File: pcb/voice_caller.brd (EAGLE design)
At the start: 100 x 80 mm, 13 parts, among them IC1 MEGA8-AI, IC2 78L12SMD, U1 AT45DB321D-S, X2 RJ45-8L-B

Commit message: Who knows
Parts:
- removed C4: (no value), rcl:C1206K
- removed IC1: MEGA8-AI, atmel:TQFP32-08
- removed R3: 220, rcl:M1206
- U$1: value MAX4544-EUTSOT23-6 -> NANO-NOISP; device max4544:SOT23-6L -> Arduino-clone:NANO-NOISP
- moved U$1 28.1 mm to (-9.80, 20.2)
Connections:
- removed net AUDIO: U$1.6
- removed net AVCC: IC1.18
- removed net MIC_IN: U$1.4
- removed net MIC_OUT: U$1.5
- removed net MIC_SWITCH: U$1.1
- removed net N$2: C4.1, R3.1, U$1.2
- net +5V: no longer IC1.4, IC1.6, R3.2
- net FLASH_CS: no longer IC1.14
- net GND: no longer C4.2, IC1.21, IC1.3, IC1.5, U$1.3
- net MISO: no longer IC1.16
- net MOSI: no longer IC1.15
- net SCK: no longer IC1.17
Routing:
- net GND: track 39.8 -> 10.6 mm
- net SCK: track 15.2 -> 6.50 mm
- net +5V: track 15.5 -> 9.25 mm
- net MISO: track 14.5 -> 8.95 mm
- net FLASH_CS: track 26.2 -> 22.6 mm
- net MOSI: track 17.9 -> 15.6 mm
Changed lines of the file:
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@@
 <?xml version="1.0" encoding="utf-8"?>
 <!DOCTYPE eagle SYSTEM "eagle.dtd">
-<eagle version="7.1.0">
+<eagle version="7.7.0">
 <drawing>
 <settings>
@@
 <element name="C1" library="rcl" package="C1206K" value="" x="26.36" y="45.6" rot="R90"/>
 <element name="C2" library="rcl" package="C1206K" value="" x="51.579403125" y="30.948178125" rot="R270"/>
-<element name="IC1" library="atmel" package="TQFP32-08" value="MEGA8-AI" x="29.43" y="31">
-<attribute name="OC_NEWARK" value="73M8863" x="29.43" y="31" size="1.778" layer="27" display="off"/>
-<attribute name="MPN" value="ATMEGA8-16AU" x="29.43" y="31" size="1.778" layer="27" display="off"/>
-<attribute name="MF" value="" x="29.43" y="31" size="1.778" layer="27" display="off"/>
-<attribute name="OC_FARNELL" value="9171371" x="29.43" y="31" size="1.778" layer="27" display="off"/>
-</element>
 <element name="U1" library="memory-atmel" package="SO08-8S2" value="AT45DB321D-S" x="47.02" y="31.05"/>
 <element name="CONN_RADIO" library="con-tycoelectronics" package="RJ45-NO-SHIELD" value="RJ45-8L-B" x="18.59" y="56.51" rot="R180">
@@
 <element name="R1" library="rcl" package="M1206" value="3k9" x="41.4" y="40.8"/>
 <element name="R2" library="rcl" package="M1206" value="2k2" x="28.4" y="40.8" rot="R180"/>
-<element name="U$1" library="max4544" package="SOT23-6L" value="MAX4544-EUTSOT23-6" x="14.6" y="34.2"/>
-<element name="R3" library="rcl" package="M1206" value="220" x="18.8" y="20.8"/>
-<element name="C4" library="rcl" package="C1206K" value="" x="12.2" y="22.2" rot="R180"/>
+<element name="U$1" library="Arduino-clone" package="NANO-NOISP" value="NANO-NOISP" x="-9.8" y="20.2"/>
 </elements>
 <signals>
-<signal name="AVCC">
-<contactref element="IC1" pad="18"/>
-</signal>
 <signal name="+5V">
-<contactref element="IC1" pad="4"/>
-<contactref element="IC1" pad="6"/>
 <contactref element="C2" pad="1"/>
 <contactref element="U1" pad="6"/>
-<wire x1="25.1374" y1="29.8" x2="22" y2="29.8" width="0.4064" layer="1"/>
 <wire x1="22" y1="29.8" x2="22" y2="31.4" width="0.4064" layer="1"/>
-<wire x1="22" y1="31.4" x2="25.1374" y2="31.4" width="0.4064" layer="1"/>
 <contactref element="C3" pad="1"/>
 <wire x1="20.2" y1="29.5" x2="21.7" y2="29.5" width="0.4064" layer="1"/>
@@
 <wire x1="48.551821875" y1="32.448178125" x2="47.655" y2="33.345" width="0.4064" layer="1"/>
 <wire x1="47.655" y1="34.775" x2="47.655" y2="33.345" width="0.4064" layer="1"/>
-<contactref element="R3" pad="2"/>
-<wire x1="25.1374" y1="31.4" x2="47.655" y2="33.345" width="0" layer="19" extent="1-1"/>
-<wire x1="20.2" y1="20.8" x2="20.2" y2="29.5" width="0" layer="19" extent="1-1"/>
+<wire x1="22" y1="31.4" x2="47.655" y2="33.345" width="0" layer="19" extent="1-1"/>
 </signal>
 <signal name="GND">
-<contactref element="IC1" pad="3"/>
-<contactref element="IC1" pad="5"/>
 <contactref element="C1" pad="2"/>
 <contactref element="C2" pad="2"/>
-<contactref element="IC1" pad="21"/>
 <contactref element="U1" pad="7"/>
-<wire x1="25.1374" y1="30.6" x2="27.8" y2="30.6" width="0.4064" layer="1"/>
-<wire x1="27.8" y1="30.6" x2="27.8" y2="31.4" width="0.4064" layer="1"/>
-<wire x1="27.8" y1="31.4" x2="27.8" y2="32.2" width="0.4064" layer="1"/>
-<wire x1="27.8" y1="32.2" x2="25.1374" y2="32.2" width="0.4064" layer="1"/>
-<wire x1="33.7226" y1="31.4" x2="27.8" y2="31.4" width="0.4064" layer="1"/>
-<wire x1="33.7226" y1="31.4" x2="45.4" y2="31.4" width="0.4064" layer="1"/>
 <wire x1="45.4" y1="31.4" x2="46.385" y2="32.385" width="0.4064" layer="1"/>
 <wire x1="46.385" y1="34.775" x2="46.385" y2="32.385" width="0.4064" layer="1"/>
 <contactref element="C3" pad="2"/>
-<wire x1="25.1374" y1="32.2" x2="20.5" y2="32.2" width="0.4064" layer="1"/>
 <wire x1="20.5" y1="32.2" x2="20.2" y2="32.5" width="0.4064" layer="1"/>
 <wire x1="51.579403125" y1="29.448178125" x2="49.321821875" y2="29.448178125" width="0.4064" layer="1"/>
@@
 <contactref element="CONN_RADIO" pad="7"/>
 <contactref element="CONN_RADIO" pad="5"/>
-<contactref element="U$1" pad="3"/>
-<contactref element="C4" pad="2"/>
 <wire x1="55.965" y1="43.8" x2="57.235" y2="43.8" width="0" layer="19" extent="1-1"/>
-<wire x1="57.235" y1="38.6" x2="57.235" y2="43.8" width="0" layer="19" extent="1-1"/>
-<wire x1="55.965" y1="38.6" x2="57.235" y2="38.6" width="0" layer="19" extent="1-1"/>
-<wire x1="46.385" y1="34.775" x2="55.965" y2="38.6" width="0" layer="19" extent="1-1"/>
-<wire x1="17.955" y1="50.16" x2="55.965" y2="43.8" width="0" layer="19" extent="1-1"/>
+<wire x1="55.965" y1="38.6" x2="55.965" y2="43.8" width="0" layer="19" extent="1-1"/>
+<wire x1="57.235" y1="38.6" x2="55.965" y2="38.6" width="0" layer="19" extent="1-1"/>
+<wire x1="51.579403125" y1="29.448178125" x2="55.965" y2="38.6" width="0" layer="19" extent="1-1"/>
+<wire x1="26.36" y1="47.1" x2="46.385" y2="34.775" width="0" layer="19" extent="1-1"/>
+<wire x1="17.955" y1="50.16" x2="26.36" y2="47.1" width="0" layer="19" extent="1-1"/>
 <wire x1="15.415" y1="50.16" x2="17.955" y2="50.16" width="0" layer="19" extent="1-1"/>
-<wire x1="26.36" y1="47.1" x2="15.415" y2="50.16" width="0" layer="19" extent="1-1"/>
-<wire x1="15.55" y1="32.9" x2="20.2" y2="32.5" width="0" layer="19" extent="1-1"/>
-<wire x1="10.7" y1="22.2" x2="15.55" y2="32.9" width="0" layer="19" extent="1-1"/>
+<wire x1="20.2" y1="32.5" x2="26.36" y2="47.1" width="0" layer="19" extent="1-1"/>
 </signal>
 <signal name="VCC">
@@
 </signal>
 <signal name="MOSI">
-<contactref element="IC1" pad="15"/>
 <contactref element="U1" pad="1"/>
 <wire x1="45.115" y1="27.325" x2="45.125" y2="27.325" width="0.4064" layer="1"/>
@@
 <wire x1="41.4" y1="23.6" x2="32.2" y2="23.6" width="0.4064" layer="1"/>
 <wire x1="32.2" y1="23.6" x2="31.43" y2="24.37" width="0.4064" layer="1"/>
-<wire x1="31.43" y1="26.7074" x2="31.43" y2="24.37" width="0.4064" layer="1"/>
 </signal>
 <signal name="MISO">
-<contactref element="IC1" pad="16"/>
 <contactref element="U1" pad="8"/>
-<wire x1="32.23" y1="26.7074" x2="37.1074" y2="26.7074" width="0.4064" layer="1"/>
-<wire x1="37.1074" y1="26.7074" x2="37.6" y2="27.2" width="0.4064" layer="1"/>
 <wire x1="45.115" y1="34.775" x2="45.115" y2="33.715" width="0.4064" layer="1"/>
 <wire x1="45.115" y1="33.715" x2="44.6" y2="33.2" width="0.4064" layer="1"/>
 <wire x1="44.6" y1="33.2" x2="38" y2="33.2" width="0.4064" layer="1"/>
 <wire x1="38" y1="33.2" x2="37.6" y2="32.8" width="0.4064" layer="1"/>
-<wire x1="37.6" y1="27.2" x2="37.6" y2="32.8" width="0" layer="19" extent="1-1"/>
 </signal>
 <signal name="SCK">
-<contactref element="IC1" pad="17"/>
 <contactref element="U1" pad="2"/>
-<wire x1="33.7226" y1="28.2" x2="42.4" y2="28.2" width="0.4064" layer="1"/>
 <wire x1="42.4" y1="28.2" x2="43.8" y2="29.6" width="0.4064" layer="1"/>
 <wire x1="43.8" y1="29.6" x2="45.8" y2="29.6" width="0.4064" layer="1"/>
@@
 <signal name="FLASH_CS">
 <contactref element="U1" pad="4"/>
-<contactref element="IC1" pad="14"/>
 <wire x1="48.925" y1="27.325" x2="48.925" y2="23.925" width="0.4064" layer="1"/>
 <wire x1="48.925" y1="23.925" x2="47.4" y2="22.4" width="0.4064" layer="1"/>
 <wire x1="47.4" y1="22.4" x2="31.4" y2="22.4" width="0.4064" layer="1"/>
 <wire x1="31.4" y1="22.4" x2="30.63" y2="23.17" width="0.4064" layer="1"/>
-<wire x1="30.63" y1="26.7074" x2="30.63" y2="23.17" width="0.4064" layer="1"/>
 </signal>
 <signal name="N$7">
@@
 <contactref element="R1" pad="2"/>
 </signal>
-<signal name="N$2">
-<contactref element="U$1" pad="2"/>
-<contactref element="R3" pad="1"/>
-<contactref element="C4" pad="1"/>
-<wire x1="17.4" y1="20.8" x2="13.7" y2="22.2" width="0" layer="19" extent="1-1"/>
-<wire x1="14.6" y1="32.9" x2="17.4" y2="20.8" width="0" layer="19" extent="1-1"/>
-</signal>
-<signal name="MIC_OUT">
-<contactref element="U$1" pad="5"/>
-</signal>
-<signal name="MIC_SWITCH">
-<contactref element="U$1" pad="1"/>
-</signal>
-<signal name="AUDIO">
-<contactref element="U$1" pad="6"/>
-</signal>
-<signal name="MIC_IN">
-<contactref element="U$1" pad="4"/>
-</signal>
 <signal name="N$1">

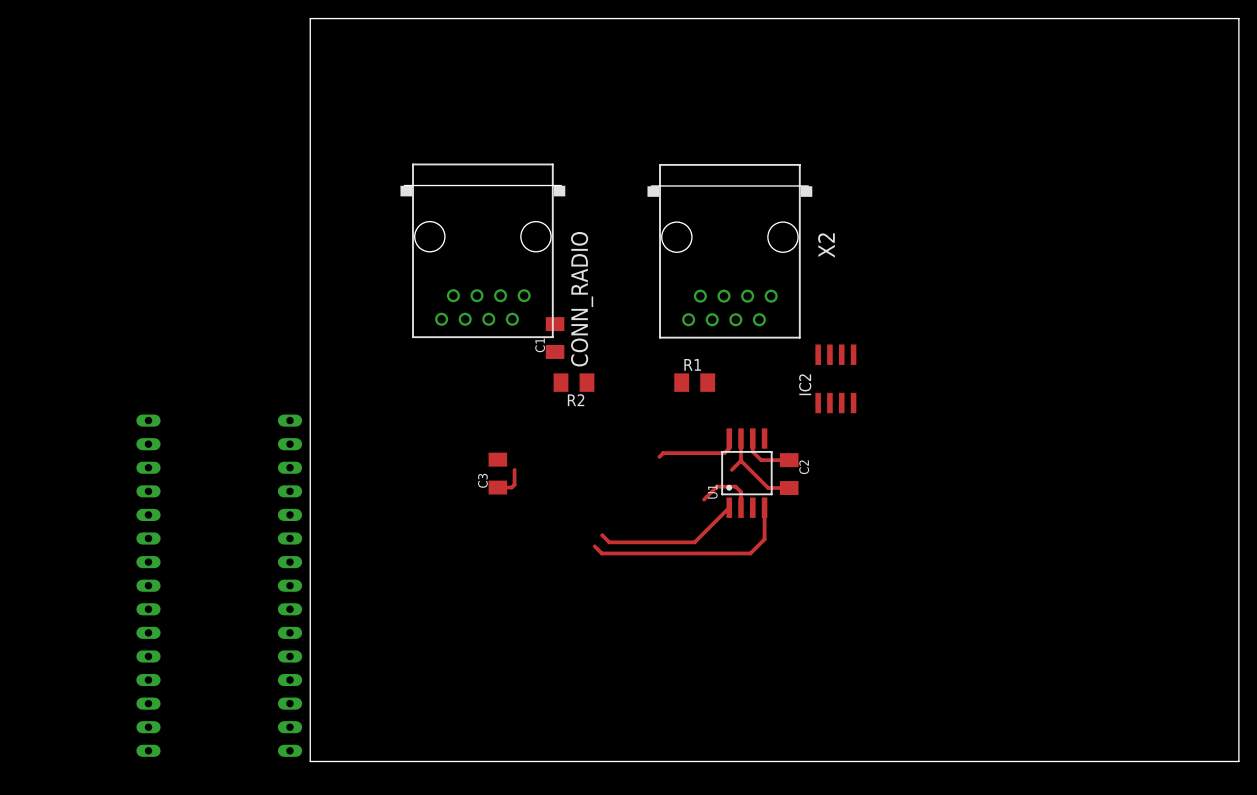
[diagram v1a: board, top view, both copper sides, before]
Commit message: Nano changed to pro micro
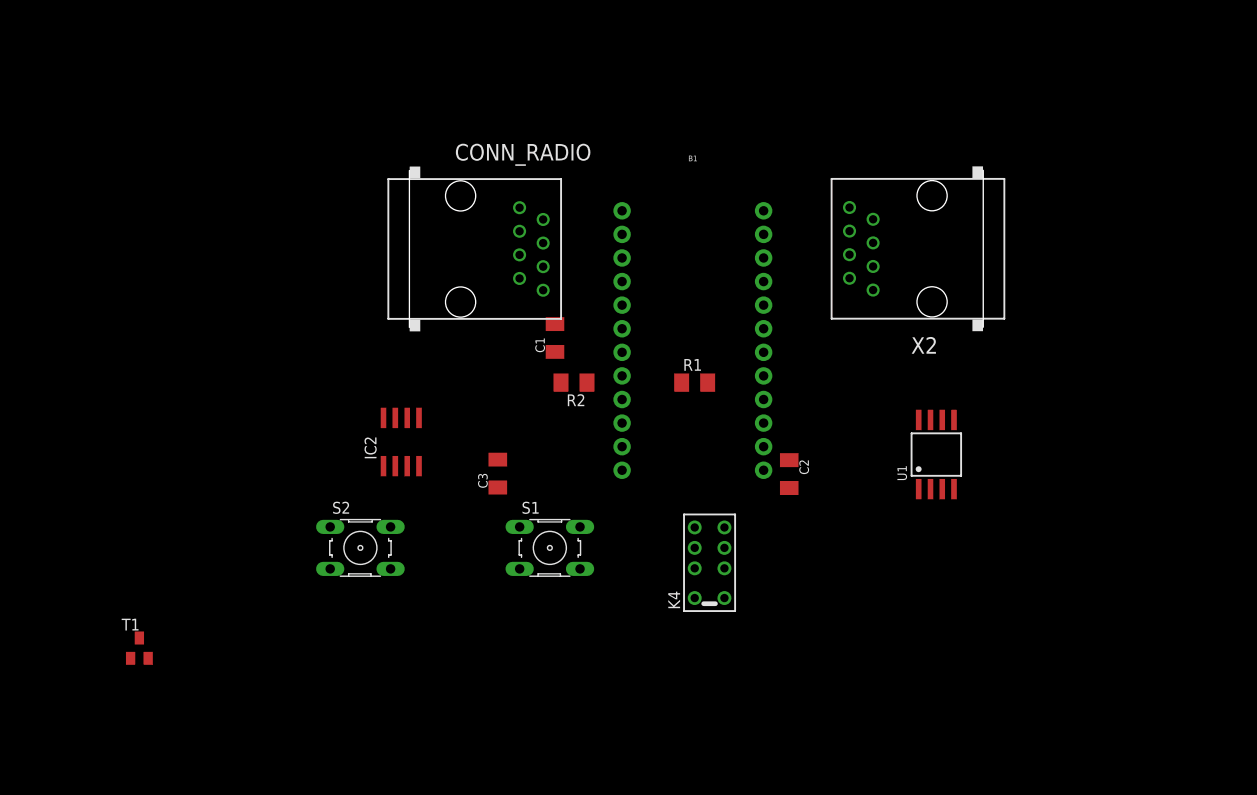
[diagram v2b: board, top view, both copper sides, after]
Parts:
- removed U$1: NANO-NOISP, Arduino-clone:NANO-NOISP
- added B1: SPARKFUN_PRO_MICRO, SparkFun-Boards:SPARKFUN_PRO_MICRO
- added K4: G6J-2P-Y, relay:G6J-2P-Y
- added S1, S2: (no value), switch-omron:B3F-10XX
- added T1: (no value), transistor:SOT23-BEC
- moved IC2 47.3 mm to (9.80, 34.4)
- moved X2 21.8 mm to (67.0, 55.2), turned to 90 degrees
- moved U1 20.5 mm to (67.4, 33.0)
- moved CONN_RADIO 2.74 mm to (16.2, 55.2), turned to 270 degrees
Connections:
- new net RAW: B1.24
- net +5V: no longer U1.6
- net GND: now also B1.23, B1.3, B1.4, S1.3, S1.4, S2.3, S2.4
- net MISO: now also B1.15
- net MOSI: now also B1.14
- net SCK: now also B1.16
- net VCC: now also B1.21, U1.6
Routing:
- net FLASH_CS: track 22.6 -> 0.00 mm
- net MOSI: track 15.6 -> 0.00 mm
- net GND: track 10.6 -> 0.42 mm
- net +5V: track 9.25 -> 0.00 mm
- net MISO: track 8.95 -> 0.00 mm
- net SCK: track 6.50 -> 0.00 mm
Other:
- board outline removed

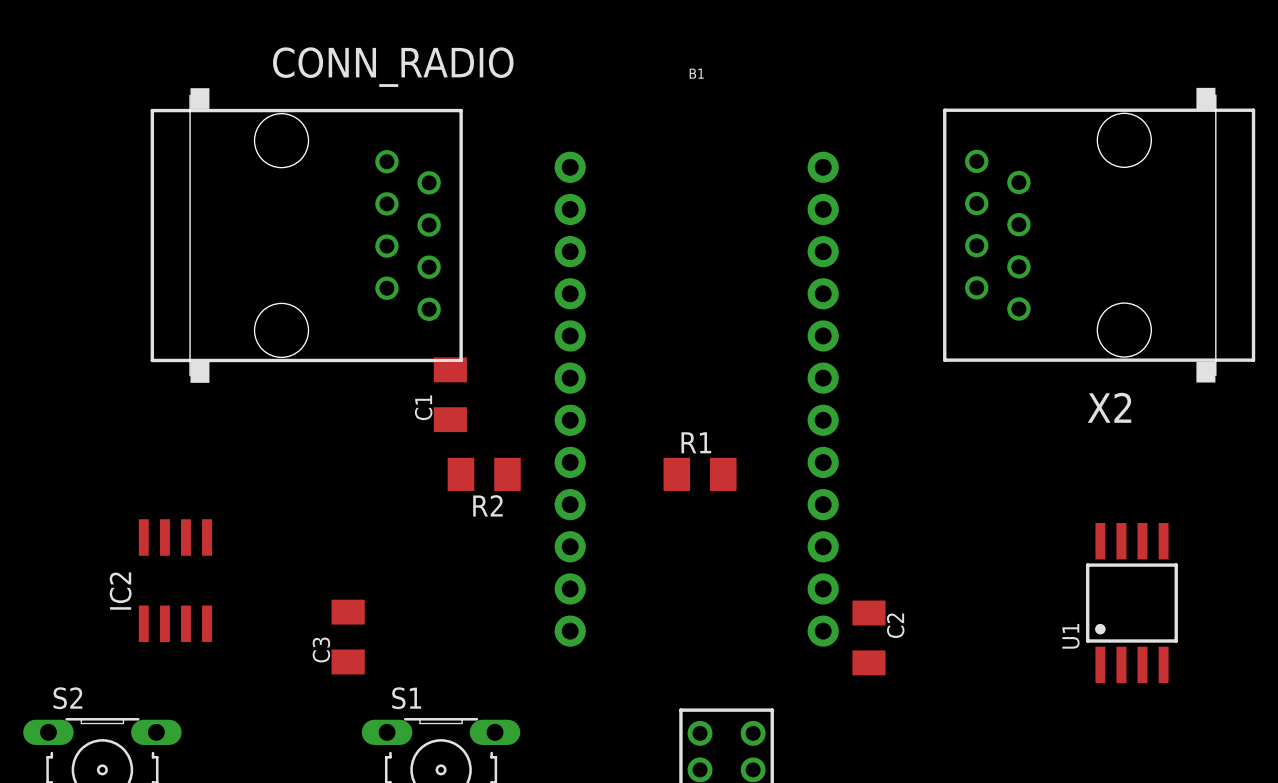
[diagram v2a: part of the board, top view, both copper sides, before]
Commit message: RJ-45 connected
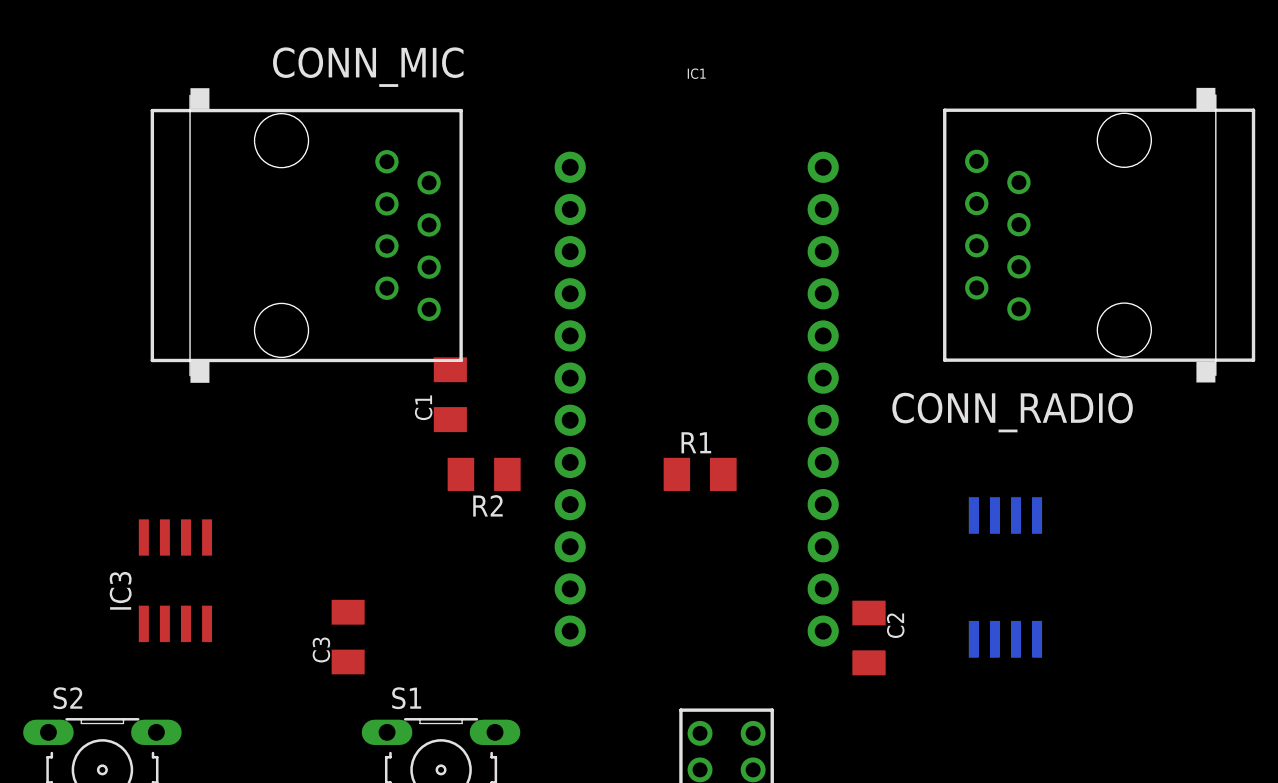
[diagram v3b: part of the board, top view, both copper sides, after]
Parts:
- removed U1: AT45DB321D-S, memory-atmel:SO08-8S2
- removed X2: RJ45-8L-B, con-tycoelectronics:RJ45-NO-SHIELD
- added CONN_MIC: RJ45-8L-B, con-tycoelectronics:RJ45-NO-SHIELD
- added IC3: 78L12SMD, linear:SO08
- IC1: value SPARKFUN_PRO_MICRO -> PRO_MICRO
- IC2: value 78L12SMD -> AT45DB321D-S; device linear:SO08 -> memory-atmel:SO08-8S2
- moved CONN_RADIO 50.8 mm to (67.0, 55.2), turned to 90 degrees
- moved IC2 50.0 mm to (59.8, 34.6), flipped to the bottom, turned to 180 degrees
- renumbered B1 to IC1
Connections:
- removed net N$1: CONN_RADIO.8, X2.8
- removed net N$10: CONN_RADIO.3
- removed net N$11: X2.3
- removed net N$12: CONN_RADIO.6
- removed net N$13: X2.6
- removed net N$9: X2.1
- new net AF_OUT: CONN_MIC.3, CONN_RADIO.3
- new net MIC: CONN_MIC.6, K4.2
- new net MIC_GND: CONN_MIC.5, K4.7
- new net MIC_GND_RADIO: CONN_RADIO.5, K4.6
- new net MIC_RADIO: CONN_RADIO.6, K4.3
- new net SQUELCH: CONN_MIC.8, CONN_RADIO.8
- net +8V: now also CONN_MIC.1
- net FLASH_CS: now also IC2.4; no longer U1.4
- net FREQ_UD: now also CONN_MIC.2
- net GND: now also CONN_MIC.7, IC3.2, IC3.3, IC3.6, IC3.7; no longer CONN_RADIO.5, CONN_RADIO.7, IC2.2, IC2.3, IC2.6, U1.7
- net MISO: now also IC2.8; no longer U1.8
- net MOSI: now also IC2.1; no longer U1.1
- net N$3: now also CONN_RADIO.7; no longer X2.7
- net N$4: now also K4.4; no longer X2.5
- net N$5: now also CONN_RADIO.4; no longer X2.4
- net N$6: now also K4.5; no longer X2.2
- net N$7: now also IC2.5; no longer U1.5
- net N$8: now also IC2.3; no longer U1.3
- net PTT: now also CONN_MIC.4; no longer CONN_RADIO.4
- net SCK: now also IC2.2; no longer U1.2
- net VCC: now also IC2.6; no longer U1.6

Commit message: Some progress with the PCB
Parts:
- added C4, C5, C6: (no value), rcl:C1206K
- added R3, R5, R6: (no value), rcl:M1206
- added R4: (no value), rcl:RTRIMT93XB
- added R7: 1k, rcl:M1206
- moved R1 72.3 mm to (-29.2, 56.1)
- moved CONN_RADIO 64.8 mm to (16.0, 15.2), turned to 270 degrees
- moved R2 58.3 mm to (-29.1, 50.9), turned to 0 degrees
- moved T1 55.3 mm to (36.1, 21.3), flipped to the bottom, turned to 180 degrees
- moved S2 53.9 mm to (58.6, 31.8)
- moved S1 43.7 mm to (57.5, 53.1)
- moved IC2 32.6 mm to (27.2, 35.0), flipped to the top, turned to 90 degrees
- moved IC3 32.4 mm to (37.7, 50.9), turned to 270 degrees
- moved C3 22.6 mm to (30.8, 50.9), turned to 270 degrees
- moved IC1 18.2 mm to (27.2, 35.0), turned to 90 degrees
- moved C1 15.6 mm to (37.8, 56.1), turned to 180 degrees
- moved K4 9.52 mm to (36.3, 14.0), turned to 270 degrees
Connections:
- removed net RAW: IC1.24
- removed net VCC: C1.1, IC1.21, IC2.6
- new net +3V3: IC1.21, IC2.6
- new net MIC_PWM: K4.4, R5.2, R6.2
- new net N$1: C4.2, R3.1
- new net N$2: C5.2, R3.2, R4.1
- new net N$9: R7.2, T1.B
- new net PWM: C4.1, IC1.13
- net +5V: now also IC1.24, IC3.1, K4.1
- net +8V: now also C1.1, IC3.8
- net GND: now also C5.1, CONN_RADIO.7, K4.5, R4.3, R6.1, T1.E
- net N$3: now also C6.2, R5.1; no longer CONN_RADIO.7
- net N$4: now also K4.8, T1.C; no longer K4.4
- net N$6: now also C6.1, R4.2; no longer K4.5
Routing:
- net GND: track 0.42 -> 124.3 mm
- net +8V: track 0.00 -> 85.6 mm, vias 0 -> 1
- net AF_OUT: track 0.00 -> 63.9 mm
- net MIC_GND: track 0.00 -> 57.3 mm
- net MIC: track 0.00 -> 45.6 mm
- net +5V: track 0.00 -> 26.8 mm
- net MISO: track 0.00 -> 21.9 mm, vias 0 -> 1
- net MIC_GND_RADIO: track 0.00 -> 16.6 mm
- net MOSI: track 0.00 -> 15.1 mm
- net SCK: track 0.00 -> 11.4 mm
- net MIC_RADIO: track 0.00 -> 10.4 mm
- net +3V3: track 0.00 -> 10.2 mm
- net N$2: track 0.00 -> 4.00 mm
- net N$1: track 0.00 -> 3.93 mm
- net PWM: track 0.00 -> 3.73 mm
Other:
- board text added: "MIC -->"
- board text added: "RADIO <--"

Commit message: More progress with the PCB
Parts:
- moved R7 33.8 mm to (33.3, 23.7), turned to 180 degrees
- moved R6 21.3 mm to (36.4, 9.68), turned to 270 degrees
- moved R5 17.5 mm to (39.4, 9.68), turned to 270 degrees
- moved C6 10.9 mm to (42.3, 9.68), turned to 90 degrees
- moved K4 4.95 mm to (31.4, 13.5)
- moved R4 3.48 mm to (40.3, 18.7), turned to 180 degrees
- moved T1 2.92 mm to (33.4, 20.1), flipped to the top, turned to 270 degrees
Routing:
- net FREQ_UD: track 0.00 -> 43.5 mm
- net SQUELCH: track 0.00 -> 41.3 mm, vias 0 -> 1
- net GND: track 124.3 -> 160.9 mm
- net N$6: track 0.00 -> 13.1 mm
- net N$2: track 4.00 -> 15.4 mm
- net MIC_PWM: track 0.00 -> 10.6 mm
- net MIC_GND_RADIO: track 16.6 -> 12.0 mm
- net MIC_RADIO: track 10.4 -> 5.69 mm
- net N$4: track 0.00 -> 4.22 mm
- net N$3: track 0.00 -> 2.96 mm
- net N$9: track 0.00 -> 2.77 mm
- net MIC_GND: track 57.3 -> 54.7 mm, vias 0 -> 1
- net MIC: track 45.6 -> 44.1 mm
